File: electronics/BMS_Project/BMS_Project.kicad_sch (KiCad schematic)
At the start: 0 parts

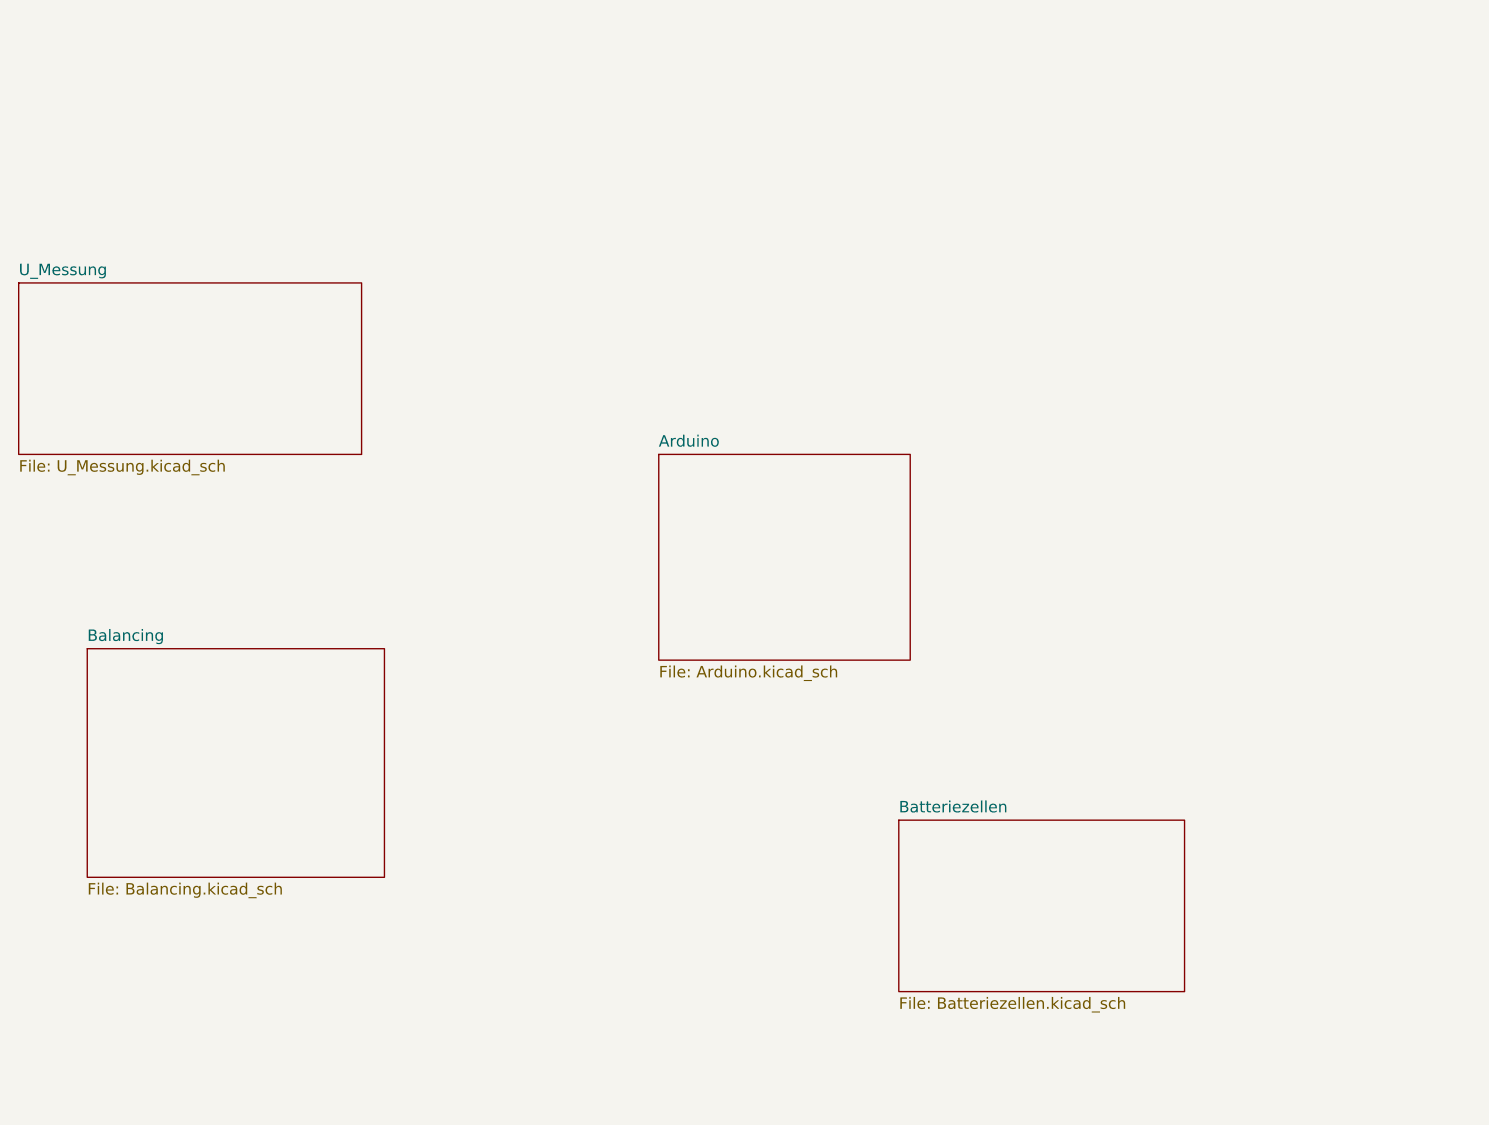
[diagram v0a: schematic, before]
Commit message: Started working on schematic segmentation and added first labels
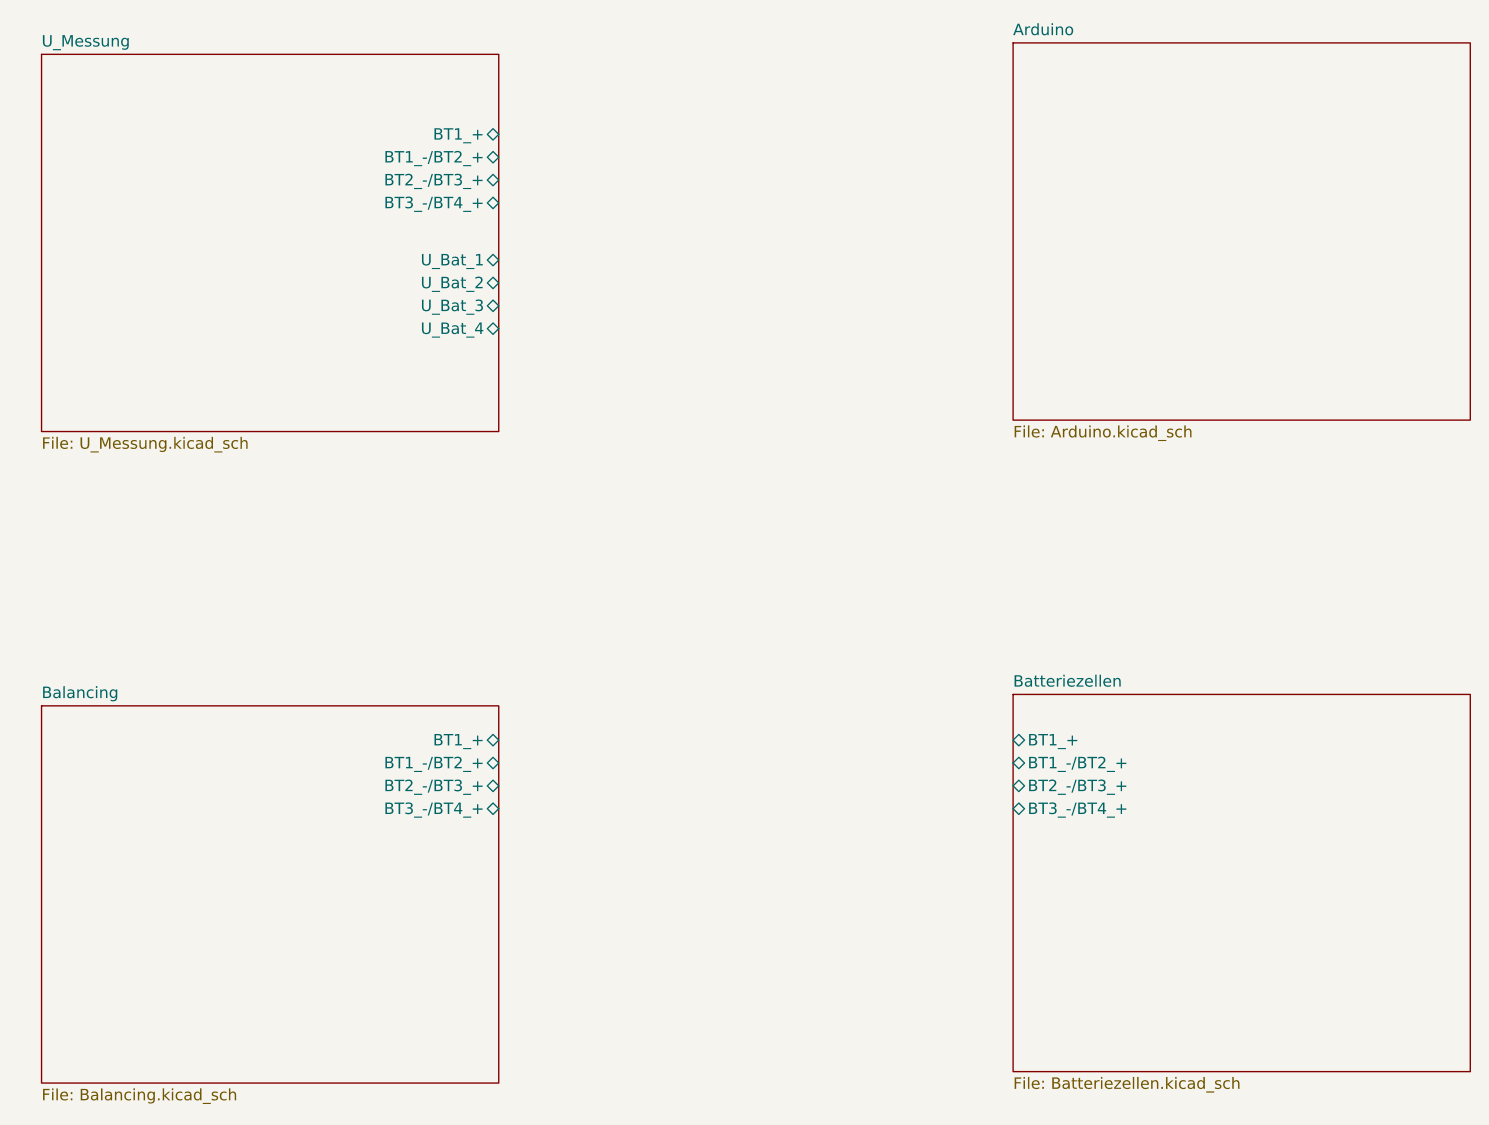
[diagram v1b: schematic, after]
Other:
- sheet Balancing ports: added BT1_+, BT1_-/BT2_+, BT2_-/BT3_+, BT3_-/BT4_+; removed none
- sheet Batteriezellen ports: added BT1_+, BT1_-/BT2_+, BT2_-/BT3_+, BT3_-/BT4_+; removed none
- sheet U_Messung ports: added BT1_+, BT1_-/BT2_+, BT2_-/BT3_+, BT3_-/BT4_+, U_Bat_1, U_Bat_2, U_Bat_3, U_Bat_4; removed none
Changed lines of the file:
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@@
     (comment 2 "Edited: ")
   )
-  (sheet (at 119.38 73.66) (size 27.94 22.86) (fields_autoplaced)
+  (sheet (at 158.75 27.94) (size 50.8 41.91) (fields_autoplaced)
     (stroke (width 0.1524) (type solid))
     (fill (color 0 0 0 0.0000))
-    (property "Sheetname" "Arduino" (at 119.38 72.9484 0)
+    (property "Sheetname" "Arduino" (at 158.75 27.2284 0)
       (effects (font (size 1.27 1.27)) (justify left bottom))
     )
-    (property "Sheetfile" "Arduino.kicad_sch" (at 119.38 97.1046 0)
+    (property "Sheetfile" "Arduino.kicad_sch" (at 158.75 70.4346 0)
       (effects (font (size 1.27 1.27)) (justify left top))
     )
@@
     )
   )
-  (sheet (at 146.05 114.3) (size 31.75 19.05) (fields_autoplaced)
+  (sheet (at 158.75 100.33) (size 50.8 41.91) (fields_autoplaced)
     (stroke (width 0.1524) (type solid))
     (fill (color 0 0 0 0.0000))
-    (property "Sheetname" "Batteriezellen" (at 146.05 113.5884 0)
+    (property "Sheetname" "Batteriezellen" (at 158.75 99.6184 0)
       (effects (font (size 1.27 1.27)) (justify left bottom))
     )
-    (property "Sheetfile" "Batteriezellen.kicad_sch" (at 146.05 133.9346 0)
+    (property "Sheetfile" "Batteriezellen.kicad_sch" (at 158.75 142.8246 0)
       (effects (font (size 1.27 1.27)) (justify left top))
+    )
+    (pin "BT1_+" bidirectional (at 158.75 105.41 180)
+      (effects (font (size 1.27 1.27)) (justify left))
+    )
+    (pin "BT2_-{slash}BT3_+" bidirectional (at 158.75 110.49 180)
+      (effects (font (size 1.27 1.27)) (justify left))
+    )
+    (pin "BT3_-{slash}BT4_+" bidirectional (at 158.75 113.03 180)
+      (effects (font (size 1.27 1.27)) (justify left))
+    )
+    (pin "BT1_-{slash}BT2_+" bidirectional (at 158.75 107.95 180)
+      (effects (font (size 1.27 1.27)) (justify left))
     )
     (instances
@@
     )
   )
-  (sheet (at 55.88 95.25) (size 33.02 25.4) (fields_autoplaced)
+  (sheet (at 50.8 101.6) (size 50.8 41.91) (fields_autoplaced)
     (stroke (width 0.1524) (type solid))
     (fill (color 0 0 0 0.0000))
-    (property "Sheetname" "Balancing" (at 55.88 94.5384 0)
+    (property "Sheetname" "Balancing" (at 50.8 100.8884 0)
       (effects (font (size 1.27 1.27)) (justify left bottom))
     )
-    (property "Sheetfile" "Balancing.kicad_sch" (at 55.88 121.2346 0)
+    (property "Sheetfile" "Balancing.kicad_sch" (at 50.8 144.0946 0)
       (effects (font (size 1.27 1.27)) (justify left top))
+    )
+    (pin "BT1_+" bidirectional (at 101.6 105.41 0)
+      (effects (font (size 1.27 1.27)) (justify right))
+    )
+    (pin "BT1_-{slash}BT2_+" bidirectional (at 101.6 107.95 0)
+      (effects (font (size 1.27 1.27)) (justify right))
+    )
+    (pin "BT2_-{slash}BT3_+" bidirectional (at 101.6 110.49 0)
+      (effects (font (size 1.27 1.27)) (justify right))
+    )
+    (pin "BT3_-{slash}BT4_+" bidirectional (at 101.6 113.03 0)
+      (effects (font (size 1.27 1.27)) (justify right))
     )
     (instances
@@
     )
   )
-  (sheet (at 48.26 54.61) (size 38.1 19.05) (fields_autoplaced)
+  (sheet (at 50.8 29.21) (size 50.8 41.91) (fields_autoplaced)
     (stroke (width 0.1524) (type solid))
     (fill (color 0 0 0 0.0000))
-    (property "Sheetname" "U_Messung" (at 48.26 53.8984 0)
+    (property "Sheetname" "U_Messung" (at 50.8 28.4984 0)
       (effects (font (size 1.27 1.27)) (justify left bottom))
     )
-    (property "Sheetfile" "U_Messung.kicad_sch" (at 48.26 74.2446 0)
+    (property "Sheetfile" "U_Messung.kicad_sch" (at 50.8 71.7046 0)
       (effects (font (size 1.27 1.27)) (justify left top))
     )
+    (pin "BT3_-{slash}BT4_+" bidirectional (at 101.6 45.72 0)
+      (effects (font (size 1.27 1.27)) (justify right))
+    )
+    (pin "BT2_-{slash}BT3_+" bidirectional (at 101.6 43.18 0)
+      (effects (font (size 1.27 1.27)) (justify right))
+    )
+    (pin "BT1_+" bidirectional (at 101.6 38.1 0)
+      (effects (font (size 1.27 1.27)) (justify right))
+    )
+    (pin "U_Bat_2" bidirectional (at 101.6 54.61 0)
+      (effects (font (size 1.27 1.27)) (justify right))
+    )
+    (pin "U_Bat_1" bidirectional (at 101.6 52.07 0)
+      (effects (font (size 1.27 1.27)) (justify right))
+    )
+    (pin "BT1_-{slash}BT2_+" bidirectional (at 101.6 40.64 0)
+      (effects (font (size 1.27 1.27)) (justify right))
+    )
+    (pin "U_Bat_4" bidirectional (at 101.6 59.69 0)
+      (effects (font (size 1.27 1.27)) (justify right))
+    )
+    (pin "U_Bat_3" bidirectional (at 101.6 57.15 0)
+      (effects (font (size 1.27 1.27)) (justify right))
+    )
     (instances

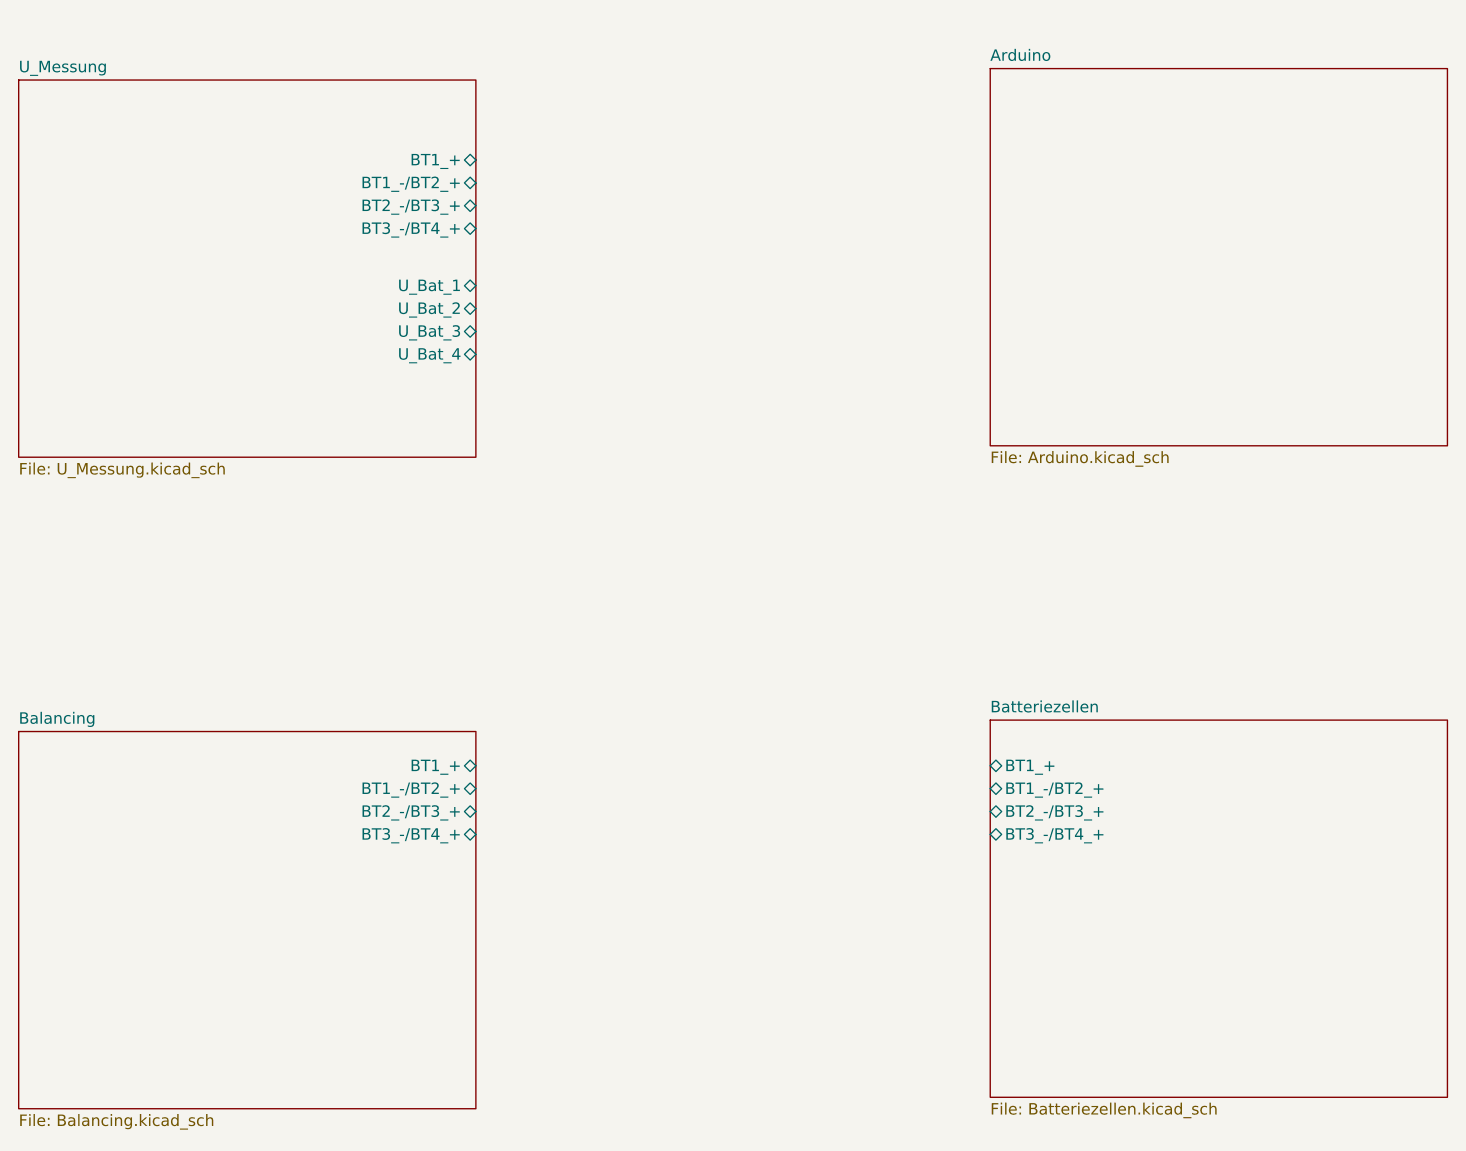
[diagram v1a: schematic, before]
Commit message: organized tasks, created ned project for cell trays
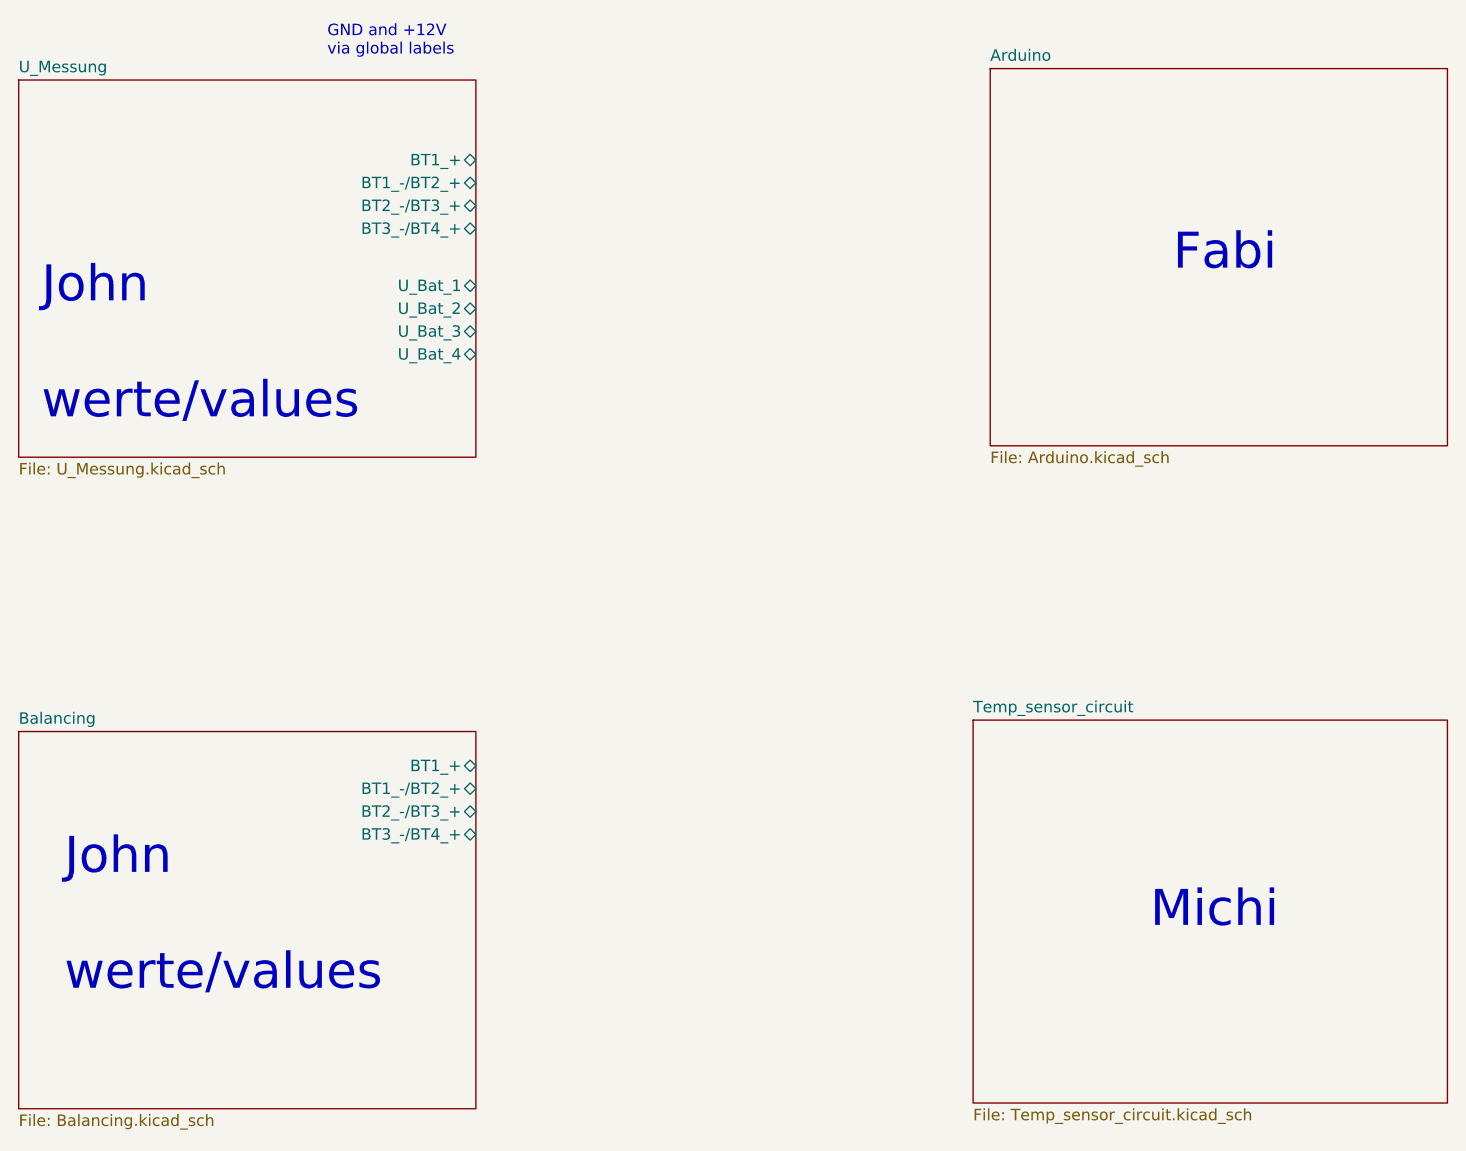
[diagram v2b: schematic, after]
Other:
- removed sheet Batteriezellen
- added sheet Temp_sensor_circuit (Temp_sensor_circuit.kicad_sch)
- note added: "Fabi"
- note added: "GND and +12V via global labels"
- note added: "John werte/values"
- note added: "Michi"
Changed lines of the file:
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@@
     (comment 2 "Edited: ")
+  )
+  (text "John\n\nwerte/values\n" (at 53.34 67.31 0)
+    (effects (font (size 4 4)) (justify left bottom))
+  )
+  (text "Fabi" (at 179.07 50.8 0)
+    (effects (font (size 4 4)) (justify left bottom))
+  )
+  (text "John\n\nwerte/values\n" (at 55.88 130.81 0)
+    (effects (font (size 4 4)) (justify left bottom))
+  )
+  (text "Michi" (at 176.53 123.825 0)
+    (effects (font (size 4 4)) (justify left bottom))
+  )
+  (text "GND and +12V\nvia global labels" (at 85.09 26.67 0)
+    (effects (font (size 1.27 1.27)) (justify left bottom))
+  )
+  (sheet (at 156.845 100.33) (size 52.705 42.545) (fields_autoplaced)
+    (stroke (width 0.1524) (type solid))
+    (fill (color 0 0 0 0.0000))
+    (property "Sheetname" "Temp_sensor_circuit" (at 156.845 99.6184 0)
+      (effects (font (size 1.27 1.27)) (justify left bottom))
+    )
+    (property "Sheetfile" "Temp_sensor_circuit.kicad_sch" (at 156.845 143.4596 0)
+      (effects (font (size 1.27 1.27)) (justify left top))
+    )
+    (instances
+      (project "BMS_Project"
+        (path "/524e7f14-feb0-4ca2-9425-a347c869bfa6" (page "5"))
+      )
+    )
   )
   (sheet (at 158.75 27.94) (size 50.8 41.91) (fields_autoplaced)
@@
       )
     )
-  )
-  (sheet (at 158.75 100.33) (size 50.8 41.91) (fields_autoplaced)
-    (stroke (width 0.1524) (type solid))
-    (fill (color 0 0 0 0.0000))
-    (property "Sheetname" "Batteriezellen" (at 158.75 99.6184 0)
-      (effects (font (size 1.27 1.27)) (justify left bottom))
-    )
-    (property "Sheetfile" "Batteriezellen.kicad_sch" (at 158.75 142.8246 0)
-      (effects (font (size 1.27 1.27)) (justify left top))
-    )
-    (pin "BT1_+" bidirectional (at 158.75 105.41 180)
-      (effects (font (size 1.27 1.27)) (justify left))
-    )
-    (pin "BT2_-{slash}BT3_+" bidirectional (at 158.75 110.49 180)
-      (effects (font (size 1.27 1.27)) (justify left))
-    )
-    (pin "BT3_-{slash}BT4_+" bidirectional (at 158.75 113.03 180)
-      (effects (font (size 1.27 1.27)) (justify left))
-    )
-    (pin "BT1_-{slash}BT2_+" bidirectional (at 158.75 107.95 180)
-      (effects (font (size 1.27 1.27)) (justify left))
-    )
-    (instances
-      (project "BMS_Project"
-        (path "/524e7f14-feb0-4ca2-9425-a347c869bfa6" (page "5"))
-      )
-    )
